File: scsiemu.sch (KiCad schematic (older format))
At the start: 56 parts, among them J1 RasPi, J2 SCSI, J3 USB_POWER, J4 POWER 5V, J5 POWER 5V, J6 AT Power 5V (171826-4), J7 I2C Ext, J8 AT Power 5V (641737-1), U1 74LS641-1, U2 74LS641-1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

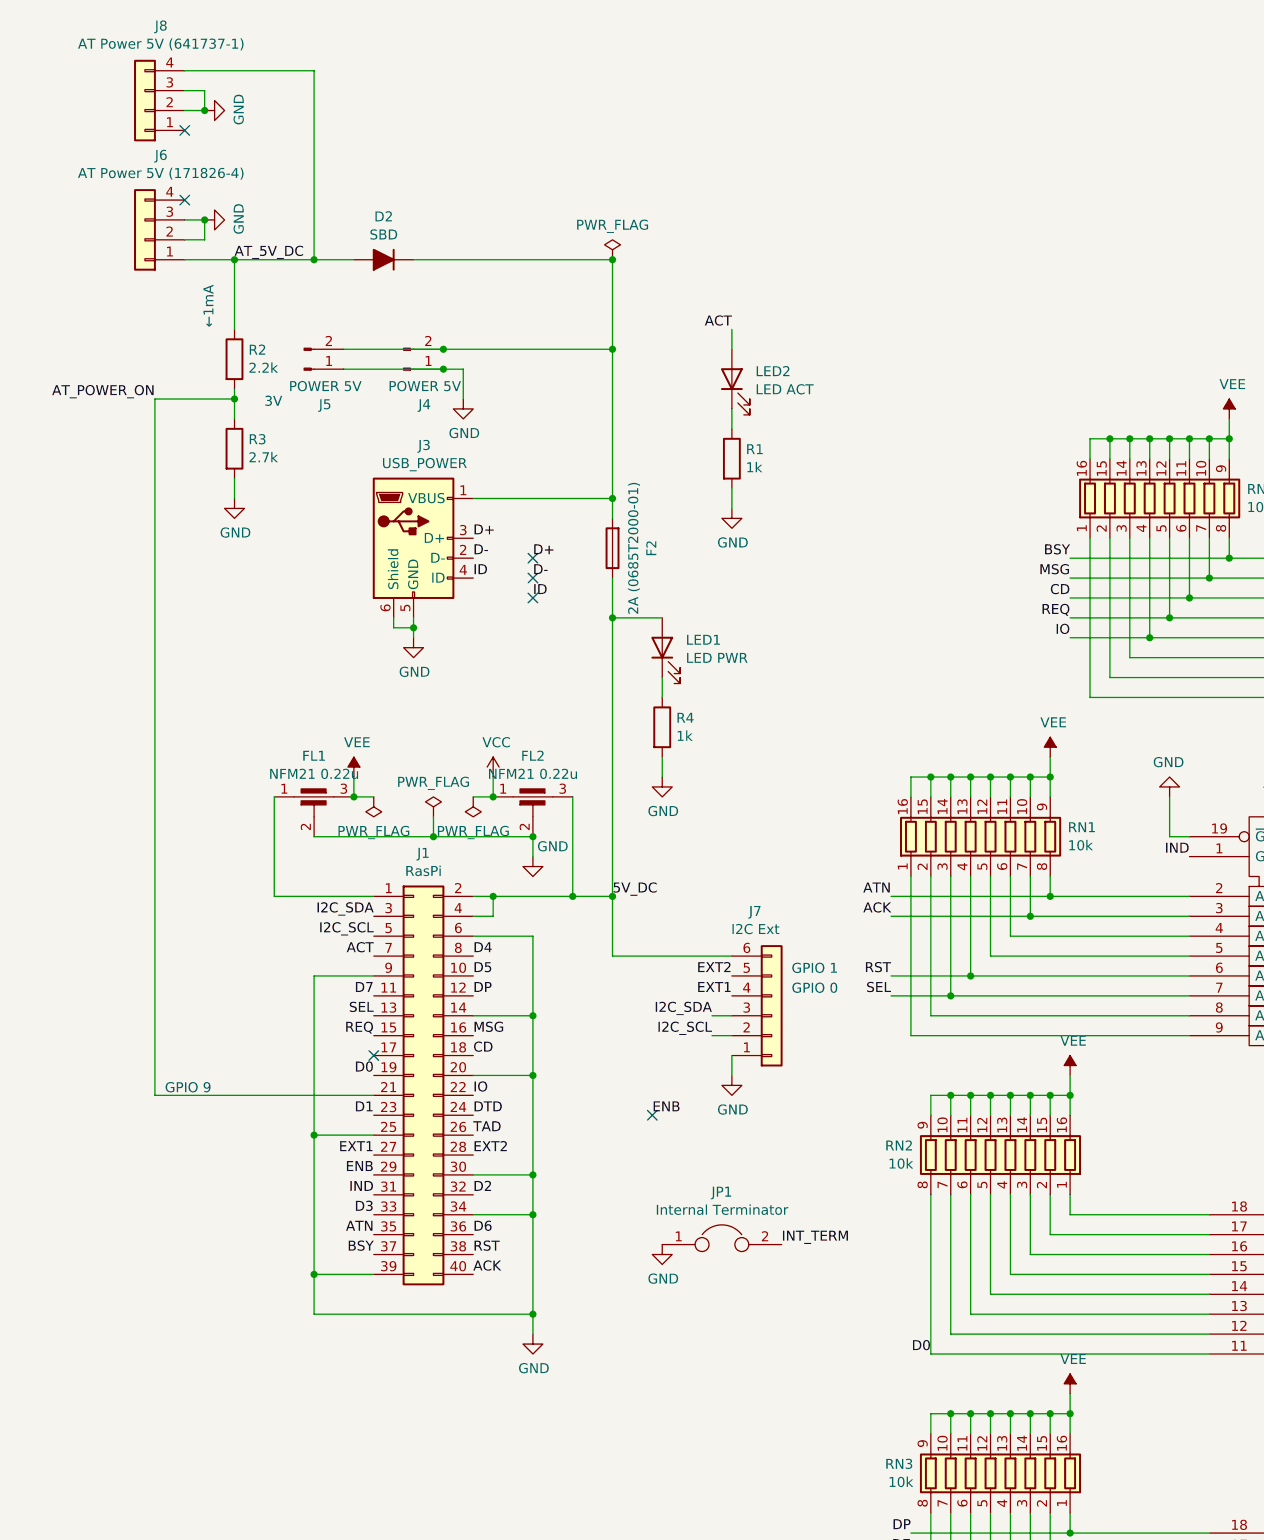
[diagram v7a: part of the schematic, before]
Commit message: add auto power off
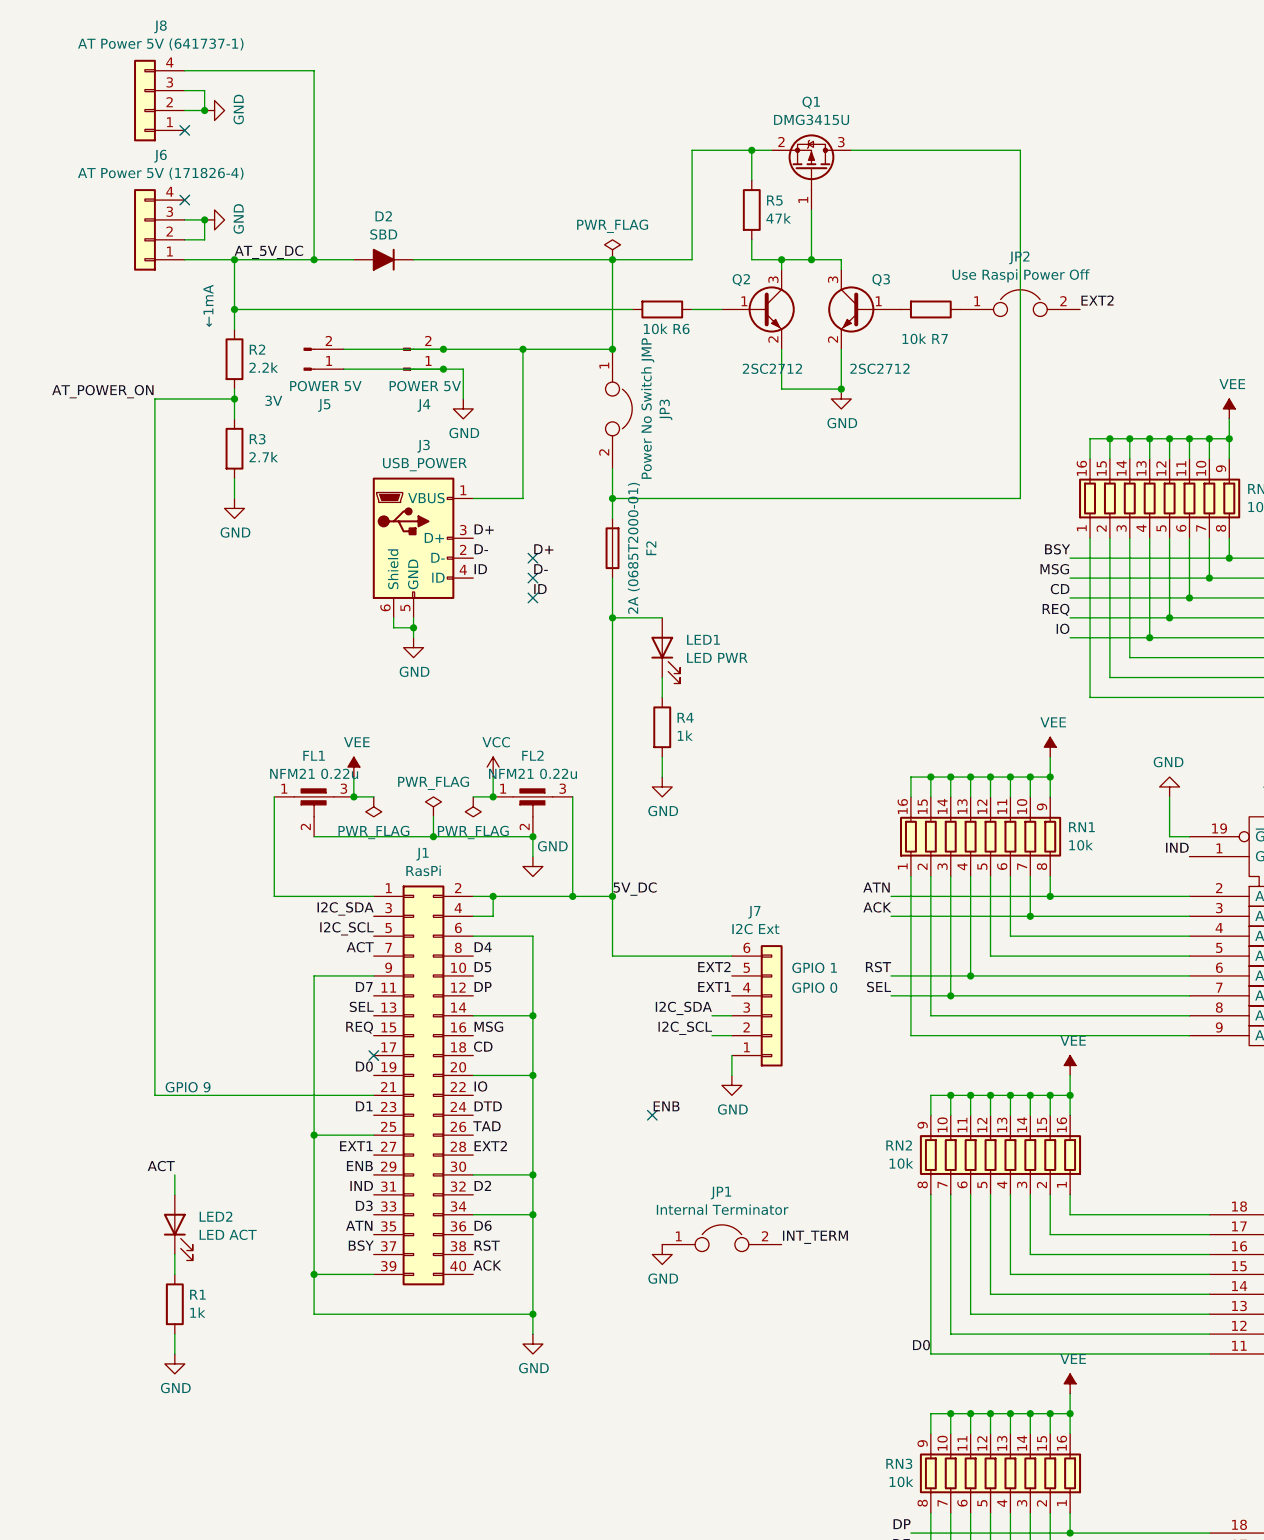
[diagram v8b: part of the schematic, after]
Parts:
- added JP2: Use Raspi Power Off, Jumper:SolderJumper-2_P1.3mm_Open_RoundedPad1.0x1.5mm, symbol Device:Jumper
- added JP3: Power No Switch JMP, Jumper:SolderJumper-2_P1.3mm_Open_RoundedPad1.0x1.5mm, symbol Device:Jumper
- added Q1: DMG3415U, Package_TO_SOT_SMD:SOT-23_Handsoldering, symbol Device:Q_PMOS_GSD
- added Q2, Q3: 2SC2712, Package_TO_SOT_SMD:SOT-23_Handsoldering, symbol Device:Q_NPN_BEC
- added R5: 47k, Resistor_SMD:R_0603_1608Metric_Pad0.98x0.95mm_HandSolder, symbol Device:R
- added R6, R7: 10k, Resistor_SMD:R_0603_1608Metric_Pad0.98x0.95mm_HandSolder, symbol Device:R
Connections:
- net AT_5V_DC: now also R6.2
- net EXT2: now also JP2.2
- net GND: now also Q2.2 (E), Q3.2 (E)
- net at D2.1 (K), J3.1 (VBUS), J4.2 (Pin_2)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: now also JP3.1, Q1.2 (S), R5.1; no longer F2.2
- new net: F2.2, JP3.2, Q1.3 (D)
- new net: Q1.1 (G), Q2.3 (C), Q3.3 (C), R5.2
- new net: Q2.1 (B), R6.1
- new net: Q3.1 (B), R7.2
- new net: JP2.1, R7.1
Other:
- moved on the sheet: LED2, R1
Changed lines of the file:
@@
 L Device:R R1
 U 1 1 5D381E27
-P 7300 2700
-F 0 "R1" H 7370 2746 50  0000 L CNN
-F 1 "1k" H 7370 2655 50  0000 L CNN
-F 2 "Resistor_SMD:R_0603_1608Metric_Pad1.05x0.95mm_HandSolder" V 7230 2700 50  0001 C CNN
-F 3 "~" H 7300 2700 50  0001 C CNN
-	1    7300 2700
+P 4500 6950
+F 0 "R1" H 4570 6996 50  0000 L CNN
+F 1 "1k" H 4570 6905 50  0000 L CNN
+F 2 "Resistor_SMD:R_0603_1608Metric_Pad1.05x0.95mm_HandSolder" V 4430 6950 50  0001 C CNN
+F 3 "~" H 4500 6950 50  0001 C CNN
+	1    4500 6950
 	1    0    0    -1
 $EndComp
@@
 L power:GND #PWR04
 U 1 1 5D48A02F
-P 7300 2950
-F 0 "#PWR04" H 7300 2700 50  0001 C CNN
-F 1 "GND" H 7305 2777 50  0000 C CNN
-F 2 "" H 7300 2950 50  0001 C CNN
-F 3 "" H 7300 2950 50  0001 C CNN
-	1    7300 2950
-	1    0    0    -1
-$EndComp
-Wire Wire Line
-	7300 2950 7300 2850
+P 4500 7200
+F 0 "#PWR04" H 4500 6950 50  0001 C CNN
+F 1 "GND" H 4505 7027 50  0000 C CNN
+F 2 "" H 4500 7200 50  0001 C CNN
+F 3 "" H 4500 7200 50  0001 C CNN
+	1    4500 7200
+	1    0    0    -1
+$EndComp
+Wire Wire Line
+	4500 7200 4500 7100
 Text Label 6000 5200 0    50   ~ 0
 D4
@@
 Connection ~ 5700 3550
 Wire Wire Line
-	6000 2900 6700 2900
-Wire Wire Line
 	6700 4900 6500 4900
 Connection ~ 6500 4900
@@
 $EndComp
 Wire Wire Line
-	6700 2900 6700 3000
-Wire Wire Line
 	6700 3300 6700 3500
 $Comp
@@
 	5950 2250 5950 2400
 Wire Wire Line
-	5850 2150 6700 2150
-Wire Wire Line
-	6700 2150 6700 2900
-Connection ~ 6700 2900
+	5850 2150 6250 2150
 $Comp
 L power:GND #PWR0102
@@
 L Device:LED LED2
 U 1 1 60304D76
-P 7300 2300
-F 0 "LED2" V 7338 2182 50  0000 R CNN
-F 1 "LED ACT" V 7247 2182 50  0000 R CNN
-F 2 "LED_SMD:LED_0603_1608Metric_Pad1.05x0.95mm_HandSolder" H 7300 2300 50  0001 C CNN
-F 3 "~" H 7300 2300 50  0001 C CNN
-	1    7300 2300
+P 4500 6550
+F 0 "LED2" V 4538 6432 50  0000 R CNN
+F 1 "LED ACT" V 4447 6432 50  0000 R CNN
+F 2 "LED_SMD:LED_0603_1608Metric_Pad1.05x0.95mm_HandSolder" H 4500 6550 50  0001 C CNN
+F 3 "~" H 4500 6550 50  0001 C CNN
+	1    4500 6550
 	0    -1   -1   0
 $EndComp
 Wire Wire Line
-	7300 2050 7300 2150
+	4500 6300 4500 6400
 $Comp
 L Device:Fuse F1
@@
 Wire Wire Line
 	6700 1700 6700 2150
-Connection ~ 6700 2150
 Wire Wire Line
 	5700 1700 6700 1700
@@
 Wire Wire Line
 	4800 2800 4800 2900
-Wire Wire Line
-	4800 2050 4800 1700
 Connection ~ 4800 1700
 Wire Wire Line
@@
 Wire Wire Line
 	5200 1700 4800 1700
-Text Label 7300 2050 2    50   ~ 0
+Text Label 4500 6300 2    50   ~ 0
 ACT
 Wire Wire Line
-	7300 2450 7300 2550
+	4500 6700 4500 6800
 $Comp
 L Device:R R4
@@
 Text Notes 4450 5900 0    50   ~ 0
 GPIO 9
+Wire Wire Line
+	6000 2900 6250 2900
+Wire Wire Line
+	6250 2900 6250 2150
+Connection ~ 6250 2150
+Wire Wire Line
+	6250 2150 6700 2150
+$Comp
+L Device:Jumper JP3
+U 1 1 6089C4B0
+P 6700 2450
+F 0 "JP3" H 6700 2714 50  0000 C CNN
+F 1 "Power No Switch JMP" H 6700 2623 50  0000 C CNN
+F 2 "Jumper:SolderJumper-2_P1.3mm_Open_RoundedPad1.0x1.5mm" H 6700 2450 50  0001 C CNN
+F 3 "~" H 6700 2450 50  0001 C CNN
+	1    6700 2450
+	0    1    1    0
+$EndComp
+Wire Wire Line
+	6700 3000 6700 2900
+Connection ~ 6700 2150
+$Comp
+L Device:Q_PMOS_GSD Q1
+U 1 1 608C32B6
+P 7700 1250
+F 0 "Q1" V 8042 1250 50  0000 C CNN
+F 1 "DMG3415U" V 7951 1250 50  0000 C CNN
+F 2 "Package_TO_SOT_SMD:SOT-23_Handsoldering" H 7900 1350 50  0001 C CNN
+F 3 "~" H 7700 1250 50  0001 C CNN
+	1    7700 1250
+	0    1    -1   0
+$EndComp
+Wire Wire Line
+	6700 1700 7100 1700
+Wire Wire Line
+	7100 1700 7100 1150
+Wire Wire Line
+	7100 1150 7400 1150
+$Comp
+L Device:R R5
+U 1 1 6093423A
+P 7400 1450
+F 0 "R5" H 7470 1496 50  0000 L CNN
+F 1 "47k" H 7470 1405 50  0000 L CNN
+F 2 "Resistor_SMD:R_0603_1608Metric_Pad0.98x0.95mm_HandSolder" V 7330 1450 50  0001 C CNN
+F 3 "~" H 7400 1450 50  0001 C CNN
+	1    7400 1450
+	1    0    0    -1
+$EndComp
+Wire Wire Line
+	7400 1300 7400 1150
+Connection ~ 7400 1150
+Wire Wire Line
+	7400 1150 7500 1150
+Wire Wire Line
+	7400 1600 7400 1700
+Wire Wire Line
+	7400 1700 7550 1700
+Wire Wire Line
+	7700 1700 7700 1450
+$Comp
+L Device:Q_NPN_BEC Q2
+U 1 1 609F27D7
+P 7450 1950
+F 0 "Q2" H 7300 2100 50  0000 L CNN
+F 1 "2SC2712" H 7350 1650 50  0000 L CNN
+F 2 "Package_TO_SOT_SMD:SOT-23_Handsoldering" H 7650 2050 50  0001 C CNN
+F 3 "~" H 7450 1950 50  0001 C CNN
+	1    7450 1950
+	1    0    0    -1
+$EndComp
+$Comp
+L Device:Q_NPN_BEC Q3
+U 1 1 609F3B32
+P 7950 1950
+F 0 "Q3" H 7800 2100 50  0000 L CNN
+F 1 "2SC2712" H 7700 1650 50  0000 L CNN
+F 2 "Package_TO_SOT_SMD:SOT-23_Handsoldering" H 8150 2050 50  0001 C CNN
+F 3 "~" H 7950 1950 50  0001 C CNN
+	1    7950 1950
+	-1   0    0    -1
+$EndComp
+Wire Wire Line
+	7550 1750 7550 1700
+Connection ~ 7550 1700
+Wire Wire Line
+	7550 1700 7700 1700
+Wire Wire Line
+	7700 1700 7850 1700
+Wire Wire Line
+	7850 1700 7850 1750
+Connection ~ 7700 1700
+Wire Wire Line
+	7550 2150 7550 2350
+Wire Wire Line
+	7550 2350 7850 2350
+Wire Wire Line
+	7850 2350 7850 2150
+$Comp
+L Device:R R7
+U 1 1 60A8FD4F
+P 8300 1950
+F 0 "R7" V 8450 1950 50  0000 L CNN
+F 1 "10k" V 8450 1800 50  0000 L CNN
+F 2 "Resistor_SMD:R_0603_1608Metric_Pad0.98x0.95mm_HandSolder" V 8230 1950 50  0001 C CNN
+F 3 "~" H 8300 1950 50  0001 C CNN
+	1    8300 1950
+	0    1    1    0
+$EndComp
+$Comp
+L Device:R R6
+U 1 1 60A9029A
+P 6950 1950
+F 0 "R6" V 7050 2000 50  0000 L CNN
+F 1 "10k" V 7050 1850 50  0000 L CNN
+F 2 "Resistor_SMD:R_0603_1608Metric_Pad0.98x0.95mm_HandSolder" V 6880 1950 50  0001 C CNN
+F 3 "~" H 6950 1950 50  0001 C CNN
+	1    6950 1950
+	0    1    1    0
+$EndComp
+$Comp
+L Device:Jumper JP2
+U 1 1 60B5D643
+P 8750 1950
+F 0 "JP2" H 8750 2214 50  0000 C CNN
+F 1 "Use Raspi Power Off" H 8750 2123 50  0000 C CNN
+F 2 "Jumper:SolderJumper-2_P1.3mm_Open_RoundedPad1.0x1.5mm" H 8750 1950 50  0001 C CNN
+F 3 "~" H 8750 1950 50  0001 C CNN
+	1    8750 1950
+	1    0    0    -1
+$EndComp
+Wire Wire Line
+	4800 1700 4800 1950
+Wire Wire Line
+	6800 1950 4800 1950
+Connection ~ 4800 1950
+Wire Wire Line
+	4800 1950 4800 2050
+Wire Wire Line
+	7100 1950 7250 1950
+$Comp
+L power:GND #PWR0106
+U 1 1 60D6FB35
+P 7850 2350
+F 0 "#PWR0106" H 7850 2100 50  0001 C CNN
+F 1 "GND" H 7855 2177 50  0000 C CNN
+F 2 "" H 7850 2350 50  0001 C CNN
+F 3 "" H 7850 2350 50  0001 C CNN
+	1    7850 2350
+	1    0    0    -1
+$EndComp
+Connection ~ 7850 2350
+Text Label 9050 1950 0    50   ~ 0
+EXT2
+Wire Wire Line
+	7900 1150 8750 1150
+Wire Wire Line
+	8750 1150 8750 2900
+Wire Wire Line
+	8750 2900 6700 2900
+Connection ~ 6700 2900
+Wire Wire Line
+	6700 2900 6700 2750
 $EndSCHEMATC
